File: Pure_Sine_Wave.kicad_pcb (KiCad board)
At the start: 2 copper layers, 134.6 x 76.2 mm, 156 parts, among them J1 SOLAR, J10 Conn_01x01_Female, J11 Conn_01x01_Female, J12 Conn_01x01_Female, J13 Conn_01x01_Female, J14 Conn_01x01_Female, J15 Conn_01x01_Female, J16 Conn_01x01_Female, J17 Conn_01x01_Female, J18 Conn_01x01_Female, J19 Conn_01x01_Female, J2 Conn_01x01_Female, J20 Conn_01x01_Female, J21 Conn_01x01_Female, J22 Conn_01x01_Female, J23 Conn_01x01_Female, J24 Conn_01x01_Female, J25 Conn_01x01_Female, J26 Conn_01x01_Female, J27 Conn_01x01_Female, J28 Conn_01x01_Female, J29 Conn_01x01_Female, J3 Conn_01x01_Female, J30 Conn_01x01_Female, J31 Conn_01x01_Female, J32 Conn_01x01_Female, J33 Conn_01x01_Female, J34 Conn_01x01_Female, J36 FAN, J38 I2C_CON, J4 Conn_01x01_Female, J5 Conn_01x01_Female, J6 Conn_01x01_Female, J7 Conn_01x01_Female, J8 BATT, J9 USB_OTG, Q1 CSD19505, Q2 CSD19505, Q3 CSD19505, Q4 Si2306, Q5 2N3904, Q6 2N3904, Q7 PMOS-100V-78A, Q8 PMOS-100V-78A, Q9 Si2306, SW1 RIGHT, SW2 LEFT, SW3 BACK, SW4 SELECT, U1 ACS712-30A, U10 ADS1015, U11 NUP4202, U12 PCF8574, U2 B1212, U3 AMS1117-5.0, U4 AMS1117-3.3, U5 XL7005A, U6 XL7005A, U7 IR2104, U8 ESP32-WROOM-32, U9 CH340C

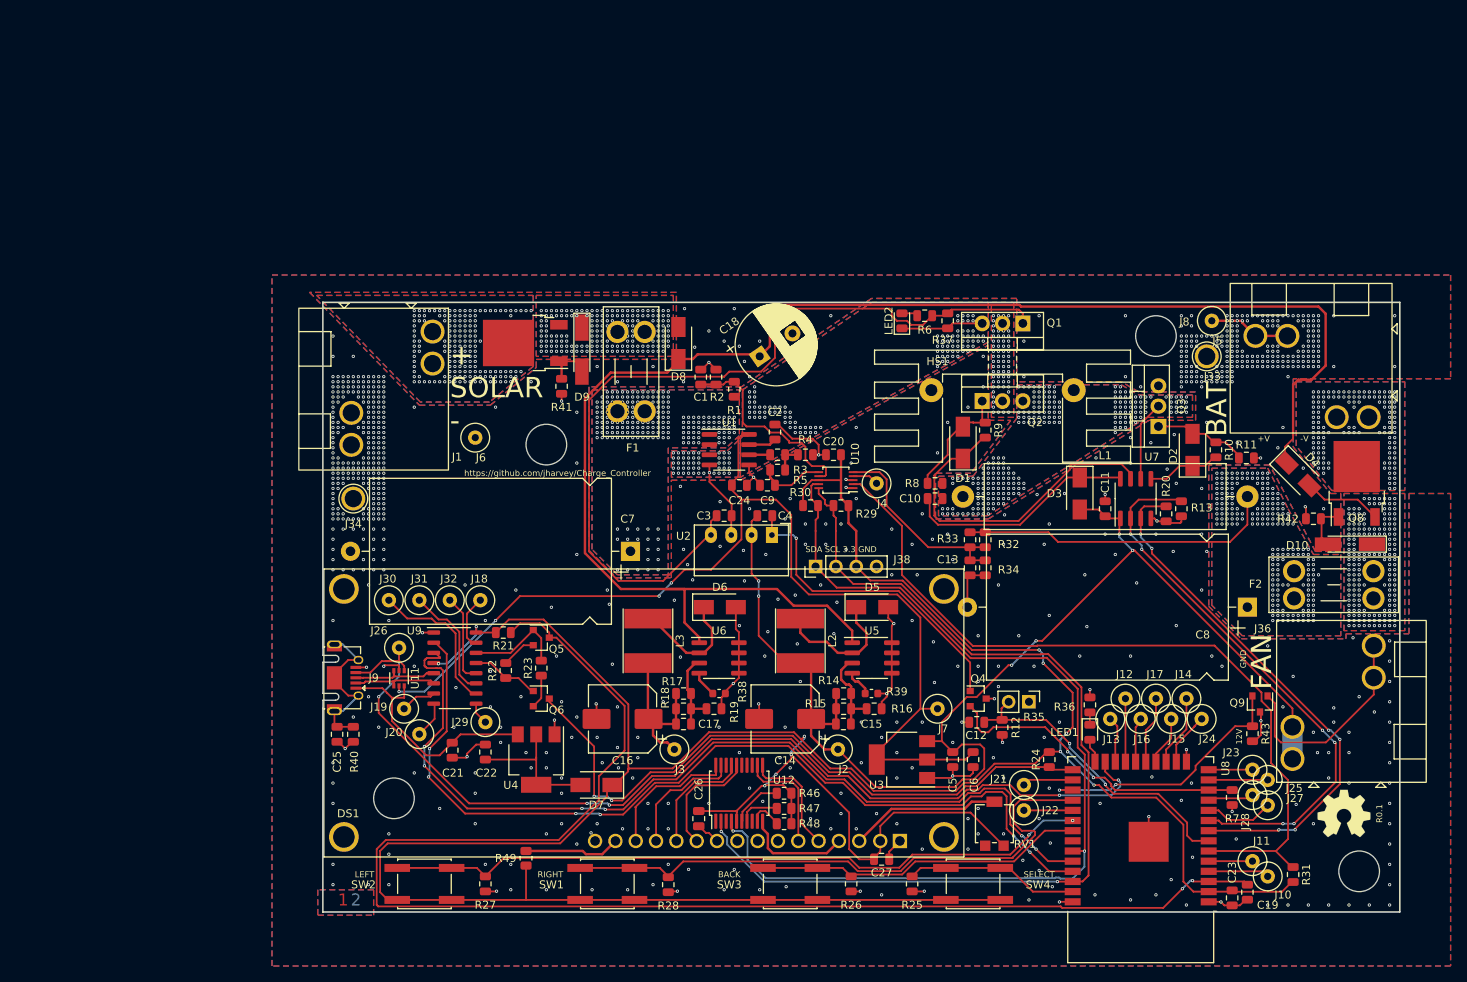
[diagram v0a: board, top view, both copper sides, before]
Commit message: Updated schematic to match changes form charge controller Added simulation for MOSFET heat predictions.
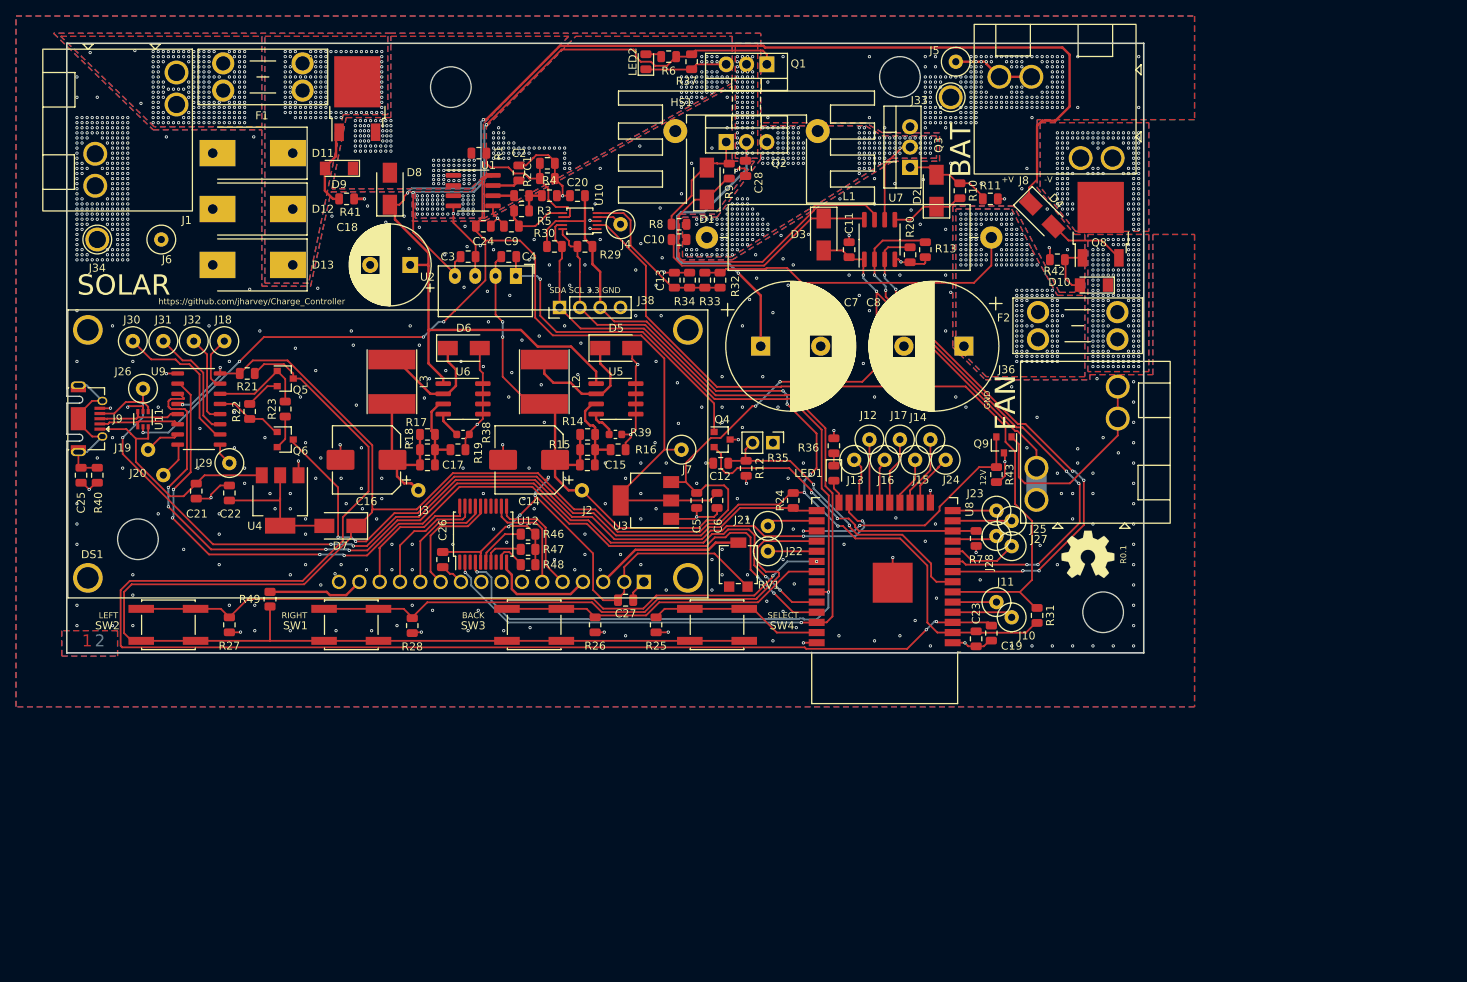
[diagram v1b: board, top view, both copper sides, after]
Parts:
- added C28: 100nf, Capacitor_SMD:C_0805_2012Metric, F.Cu at (119.3, 51.1)
- added D11: 90V-34A, Diode_SMD:D_SMC-RM10_Universal_Handsoldering, F.Cu at (57.7, 49.2)
- added D12: 120V-26A, Diode_SMD:D_SMC-RM10_Universal_Handsoldering, F.Cu at (57.7, 56.2)
- added D13: 120V-26A, Diode_SMD:D_SMC-RM10_Universal_Handsoldering, F.Cu at (57.7, 63.2)
- C7, C8: footprint Capacitor_THT:CP_Axial_L30.0mm_D18.0mm_P35.00mm_Horizontal -> Capacitor_THT:CP_Radial_D16.0mm_P7.50mm
- D10, D9: footprint Diode_SMD:D_MiniMELF_Handsoldering -> Diode_SMD:D_MiniMELF
- U1: value ACS712-30A -> Hall Amp Sense
- moved F1 65.7 mm to (54.0, 38.0), turned to 0 degrees
- moved C13 51.6 mm to (110.4, 65.1), turned to 90 degrees
- moved R34 51.6 mm to (112.3, 65.1), turned to 90 degrees
- moved C8 48.2 mm to (146.6, 73.3)
- moved J6 46.4 mm to (46.3, 60.0)
- moved R32 46.4 mm to (116.1, 65.1)
- moved R33 46.4 mm to (114.2, 65.1)
- moved C11 45.5 mm to (132.2, 61.3)
- moved D2 45.5 mm to (143.2, 53.9)
- moved J21 45.5 mm to (122.1, 95.8)
- moved J24 45.5 mm to (144.3, 87.5)
- moved LED1 45.5 mm to (130.3, 89.2)
- moved LOGO1 45.5 mm to (162.1, 99.4)
- moved R31 45.5 mm to (155.7, 107.0)
- moved R36 45.5 mm to (130.3, 85.8)
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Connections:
- C7 pad 1: /S+Fused -> /S+Fused3
- F1 pad 1: /S+Fused -> /S+
- F1 pad 2: /S+Polarity -> /S+Fused
- Q7 pad 2: /S+ -> /S+Fused
- R1 pad 1: /S+Fused -> /S+Polarity
- U1 pad 1: /S+Fused -> /S+Polarity
- U1 pad 2: /S+Fused -> /S+Polarity
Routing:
- net /S+Fused3: track 0.00 -> 40.9 mm, vias 63 -> 64
- net Net-(C3-Pad1): track 106.3 -> 75.0 mm, vias 0 -> 2
- net /S+B+1A: track 190.5 -> 172.1 mm, vias 0 -> 2
- net /A3: track 25.5 -> 18.6 mm
- net /12V: track 155.8 -> 161.5 mm
- net /A1: track 25.9 -> 21.1 mm
- net Net-(D9-Pad2): track 6.36 -> 10.1 mm
- net /B+Fused: track 39.6 -> 41.2 mm
- net Net-(D10-Pad2): track 5.84 -> 6.84 mm
- net Net-(D2-Pad2): track 11.9 -> 10.9 mm
- net /GPIO34: track 98.7 -> 99.4 mm
- net GND: track 130.9 -> 131.5 mm, vias 788 -> 765
- net /GPIO32: track 67.0 -> 67.5 mm
- net /B+Polarity: vias 173 -> 182
- net /BuckFB: vias 220 -> 225
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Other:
- outline, holes or cut-outs redrawn
- board text added: "SOLAR"
- board text removed: "+ SOLAR -"
